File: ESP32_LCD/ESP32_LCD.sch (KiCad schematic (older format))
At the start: 3 parts

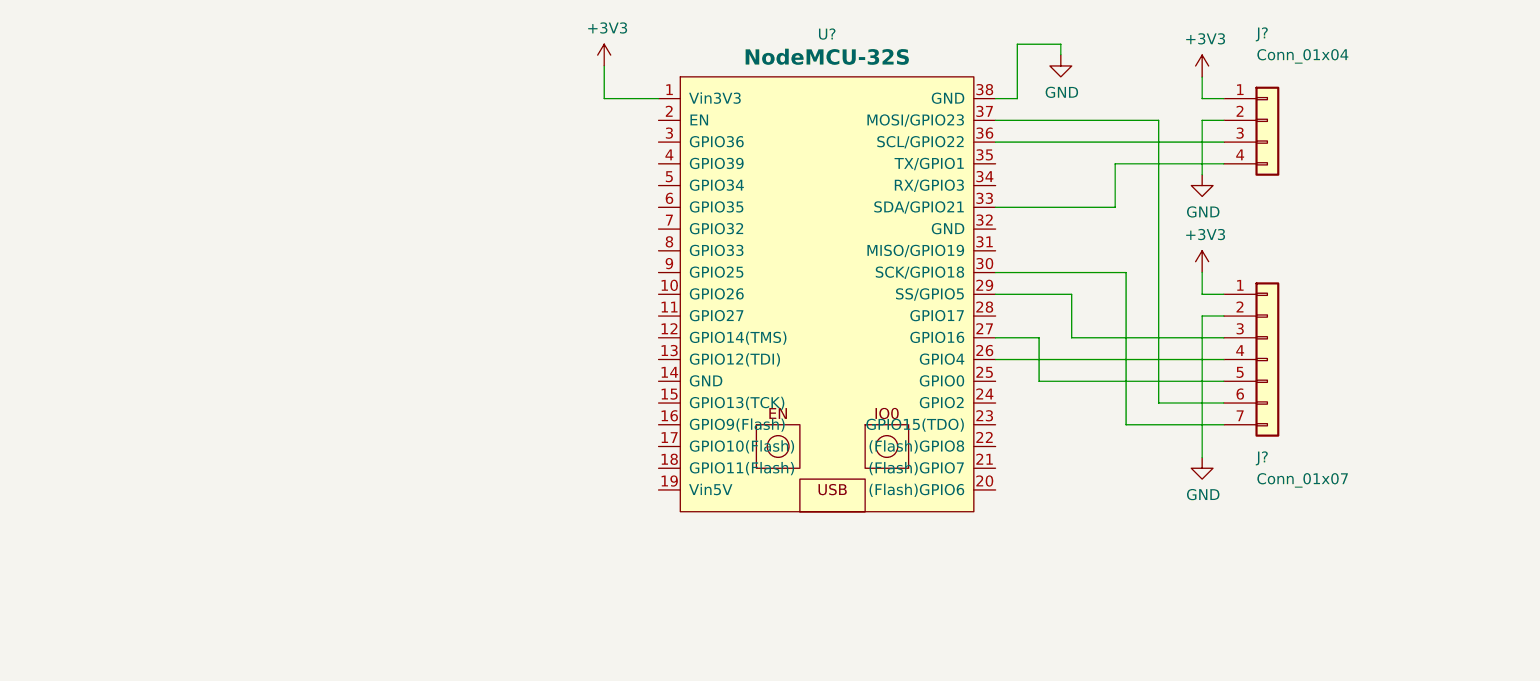
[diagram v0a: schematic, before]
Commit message: add platformio debugger
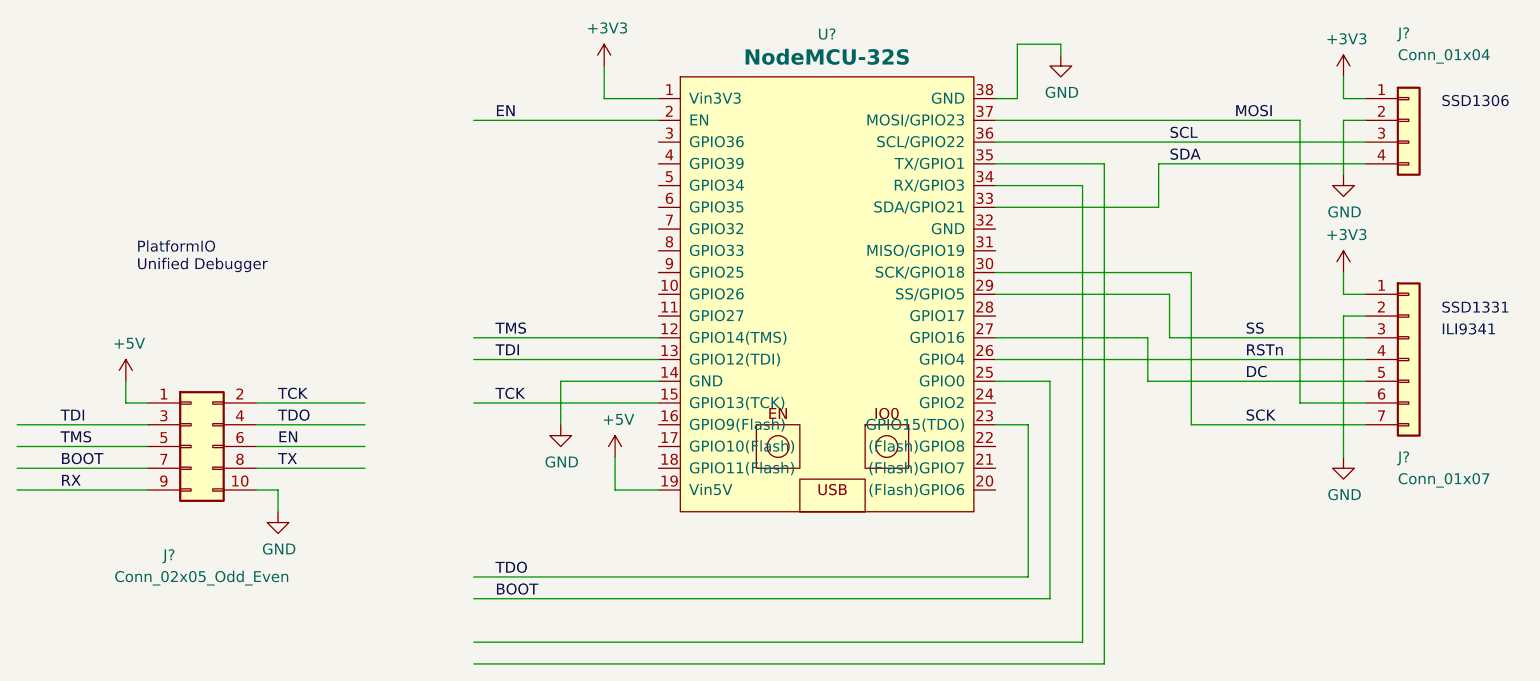
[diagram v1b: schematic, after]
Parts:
- removed U?: NodeMCU-32S, symbol kdn_kicad:NodeMCU-32S
- added J?: Conn_02x05_Odd_Even, symbol Connector_Generic:Conn_02x05_Odd_Even
- added U?: NodeMCU-32S, symbol kdn_kicad:NodeMCU-32S
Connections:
- net labels added: +5V, BOOT, DC, EN, MOSI, RSTn, RX, SCK, SCL, SDA, SS, TCK, TDI, TDO, TMS, TX
- wire segments 31 -> 63
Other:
- note added: "ILI9341"
- note added: "PlatformIO \nUnified Debugger\n"
- note added: "SSD1306\n"
- note added: "SSD1331\n"
- moved on the sheet: J?
